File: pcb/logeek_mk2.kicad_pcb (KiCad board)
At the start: 2 copper layers, 68.6 x 53.3 mm, 137 parts, among them P1 Power, P10 XH2.54-2P RA, P11 BARREL_JACK, P12 USB_B, P13 DC3 5x2, P14 Power, P15 Analog, P16 Digital, P17 Digital, P2 Analog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

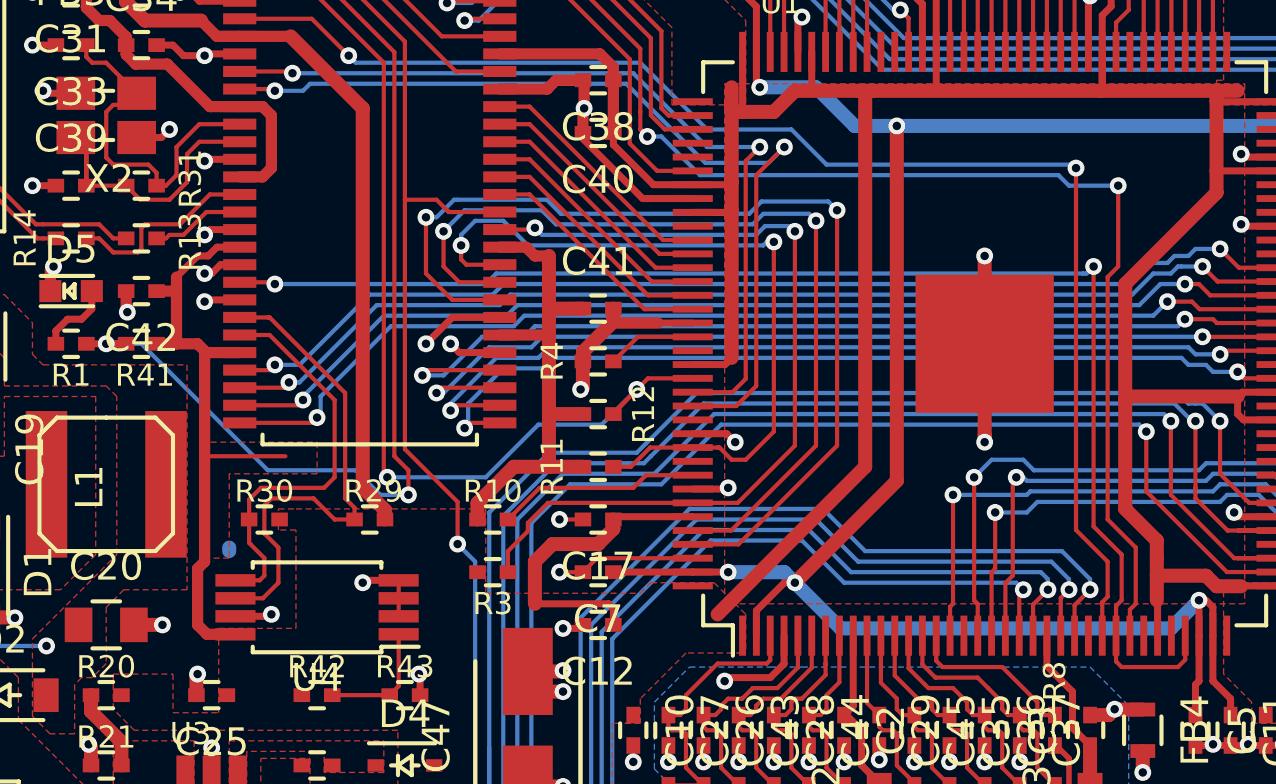
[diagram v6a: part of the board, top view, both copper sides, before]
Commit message: FPGA footprint center pad updated.
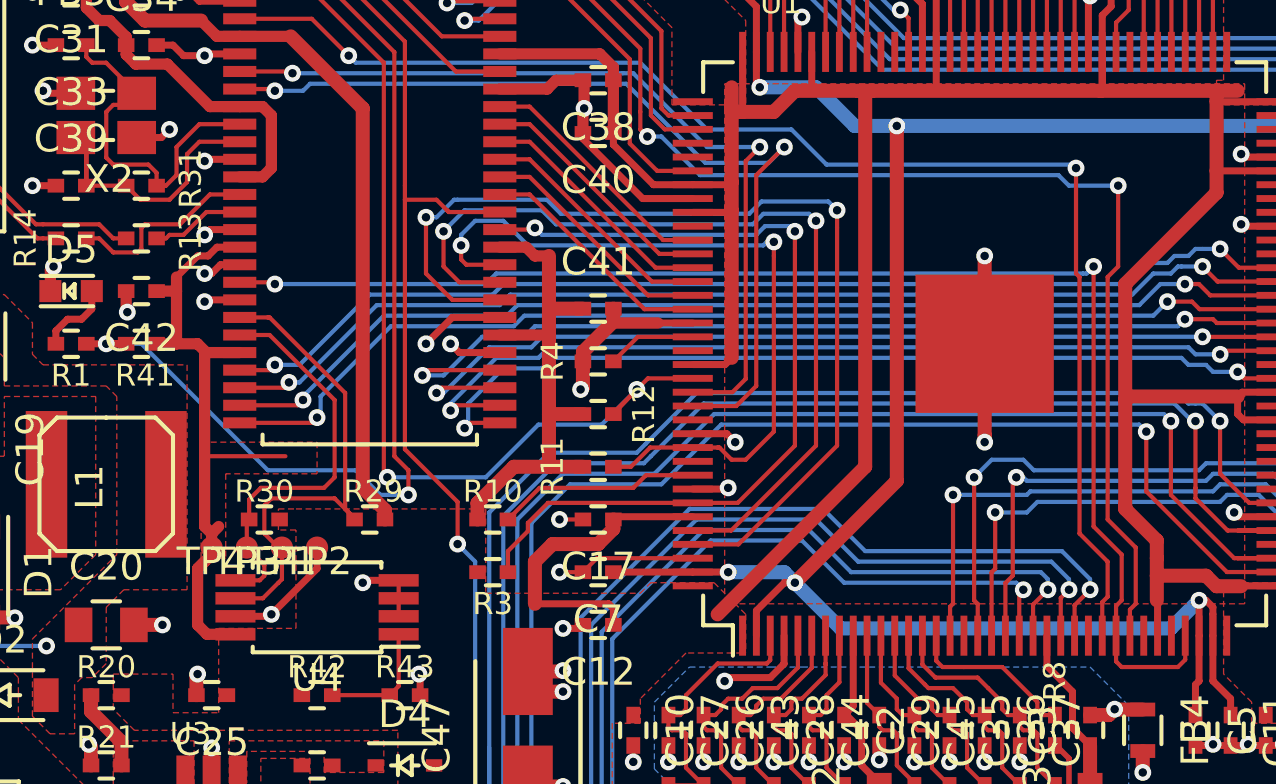
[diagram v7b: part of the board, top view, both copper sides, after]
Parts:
- added TP1: TP, Logeek_MK2:Test_Point_1Pin, F.Cu at (131.3, 105.8)
- added TP2: TP, Logeek_MK2:Test_Point_1Pin, F.Cu at (132.6, 105.8)
- added TP3: TP, Logeek_MK2:Test_Point_1Pin, F.Cu at (130.0, 105.8)
- added TP4: TP, Logeek_MK2:Test_Point_1Pin, F.Cu at (128.8, 105.8)
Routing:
- net GNDD: track 134.5 -> 172.6 mm
- net +3V3: track 287.7 -> 288.6 mm

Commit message: Silkscreen art updated.
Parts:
- moved G*** 3.81 mm to (145.3, 99.7)
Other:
- board text added: "+5V~~+24V"
- board text removed: "+5V~~+20V"
